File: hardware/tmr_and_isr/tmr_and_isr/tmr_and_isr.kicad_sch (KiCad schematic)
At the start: 21 parts, among them J0 Conn_01x10, J1 Conn_01x10, J2 Conn_01x10, J3 Conn_01x12_Male, U1 74LS04, U2 4072, U3 74LS10, U4 74HC00, U6 74HC00, U7 74LS10

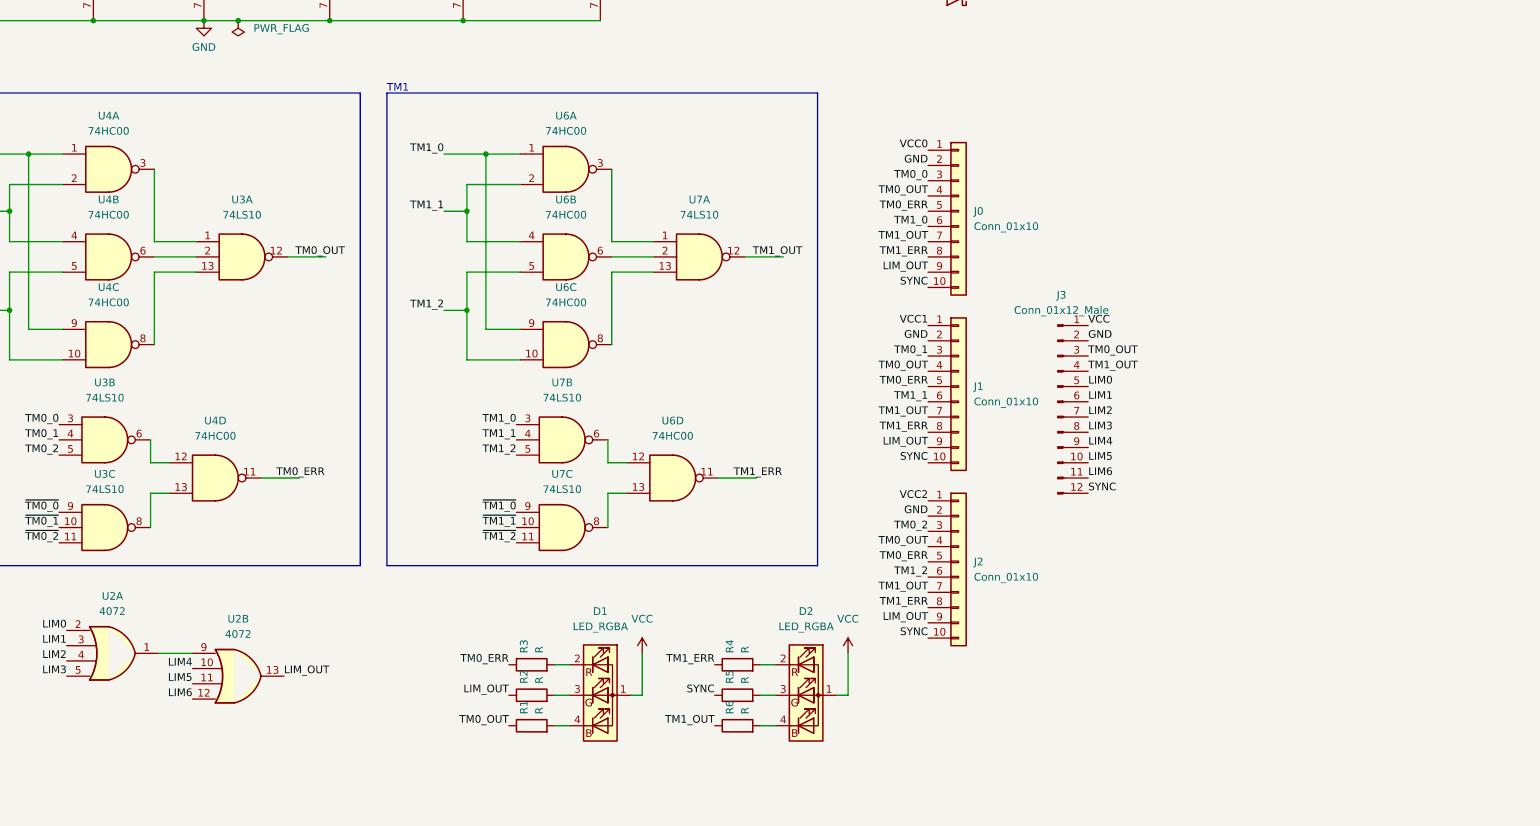
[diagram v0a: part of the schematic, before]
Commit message: Added updated TMR and ISR PCB
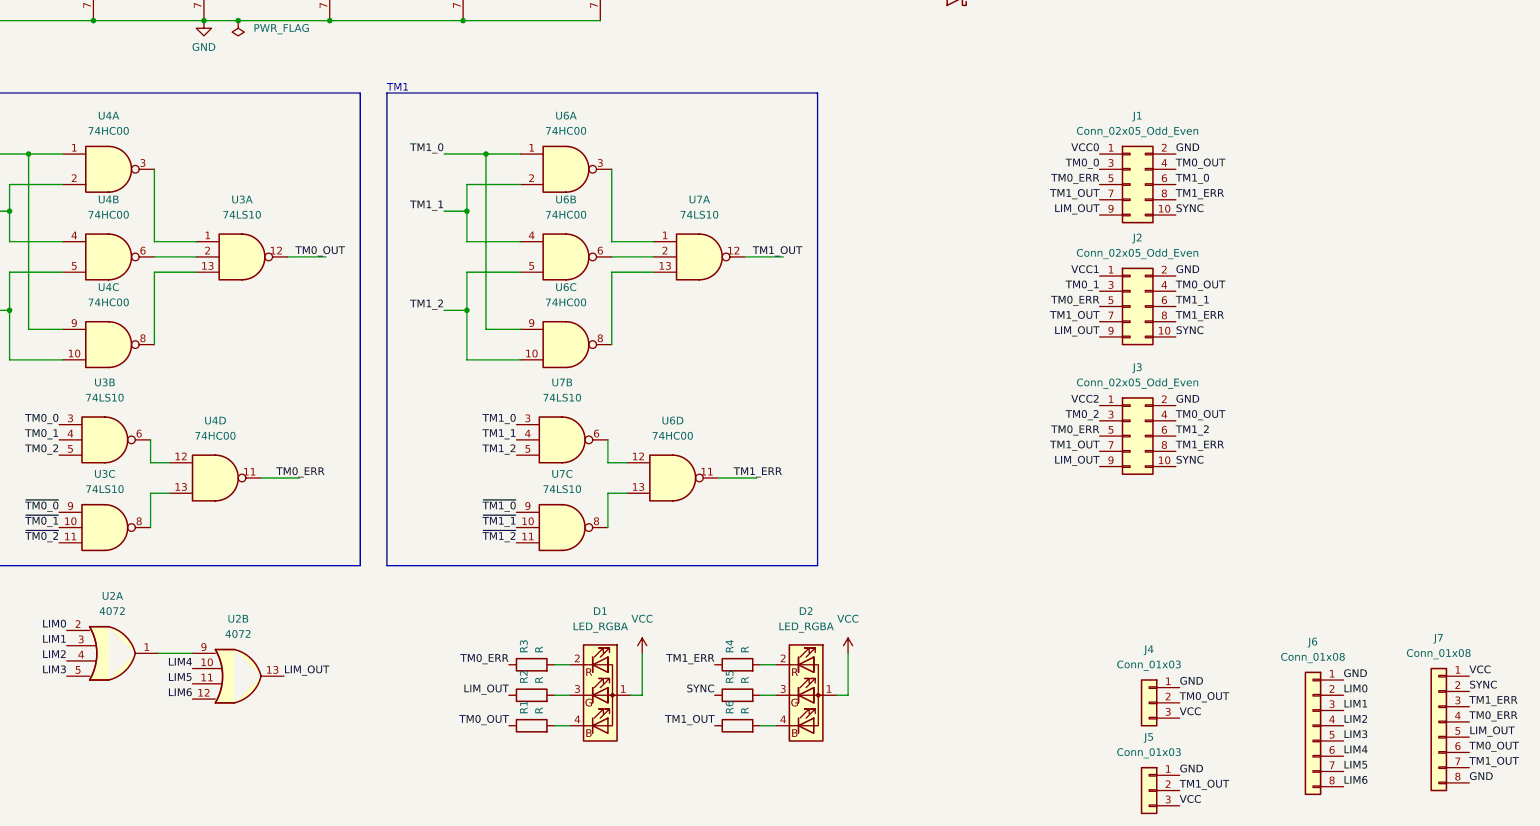
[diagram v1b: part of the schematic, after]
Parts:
- removed J0, J1, J2: Conn_01x10, Connector_JST:JST_PHD_B10B-PHDSS_2x05_P2.00mm_Vertical, symbol Connector_Generic:Conn_01x10
- removed J3: Conn_01x12_Male, Connector_JST:JST_GH_SM12B-GHS-TB_1x12-1MP_P1.25mm_Horizontal, symbol Connector:Conn_01x12_Male
- added J1, J2, J3: Conn_02x05_Odd_Even, Connector_PinSocket_2.54mm:PinSocket_2x05_P2.54mm_Vertical, symbol Connector_Generic:Conn_02x05_Odd_Even
- added J4, J5: Conn_01x03, Connector_JST:JST_PH_B3B-PH-K_1x03_P2.00mm_Vertical, symbol Connector_Generic:Conn_01x03
- added J6, J7: Conn_01x08, Connector_PinHeader_2.54mm:PinHeader_1x08_P2.54mm_Vertical, symbol Connector_Generic:Conn_01x08
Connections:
- net GND: now also J1.2 (Pin_2), J2.2 (Pin_2), J3.2 (Pin_2), J4.1 (Pin_1), J5.1 (Pin_1), J6.1 (Pin_1), J7.8 (Pin_8)
- net LIM0: now also J6.2 (Pin_2)
- net LIM1: now also J6.3 (Pin_3)
- net LIM2: now also J6.4 (Pin_4)
- net LIM3: now also J6.5 (Pin_5)
- net LIM4: now also J6.6 (Pin_6)
- net LIM5: now also J6.7 (Pin_7)
- net LIM6: now also J6.8 (Pin_8)
- net LIM_OUT: now also J1.9 (Pin_9), J2.9 (Pin_9), J3.9 (Pin_9), J7.5 (Pin_5)
- net SYNC: now also J1.10 (Pin_10), J2.10 (Pin_10), J3.10 (Pin_10), J7.2 (Pin_2)
- net TM0_0: now also J1.3 (Pin_3)
- net TM0_1: now also J2.3 (Pin_3)
- net TM0_2: now also J3.3 (Pin_3)
- net TM0_ERR: now also J1.5 (Pin_5), J2.5 (Pin_5), J3.5 (Pin_5), J7.4 (Pin_4)
- net TM0_OUT: now also J1.4 (Pin_4), J2.4 (Pin_4), J3.4 (Pin_4), J4.2 (Pin_2), J7.6 (Pin_6)
- net TM1_0: now also J1.6 (Pin_6)
- net TM1_1: now also J2.6 (Pin_6)
- net TM1_2: now also J3.6 (Pin_6)
- net TM1_ERR: now also J1.8 (Pin_8), J2.8 (Pin_8), J3.8 (Pin_8), J7.3 (Pin_3)
- net TM1_OUT: now also J1.7 (Pin_7), J2.7 (Pin_7), J3.7 (Pin_7), J5.2 (Pin_2), J7.7 (Pin_7)
- net VCC: now also J4.3 (Pin_3), J5.3 (Pin_3), J7.1 (Pin_1)
- net VCC0: now also J1.1 (Pin_1)
- net VCC1: now also J2.1 (Pin_1)
- net VCC2: now also J3.1 (Pin_1)

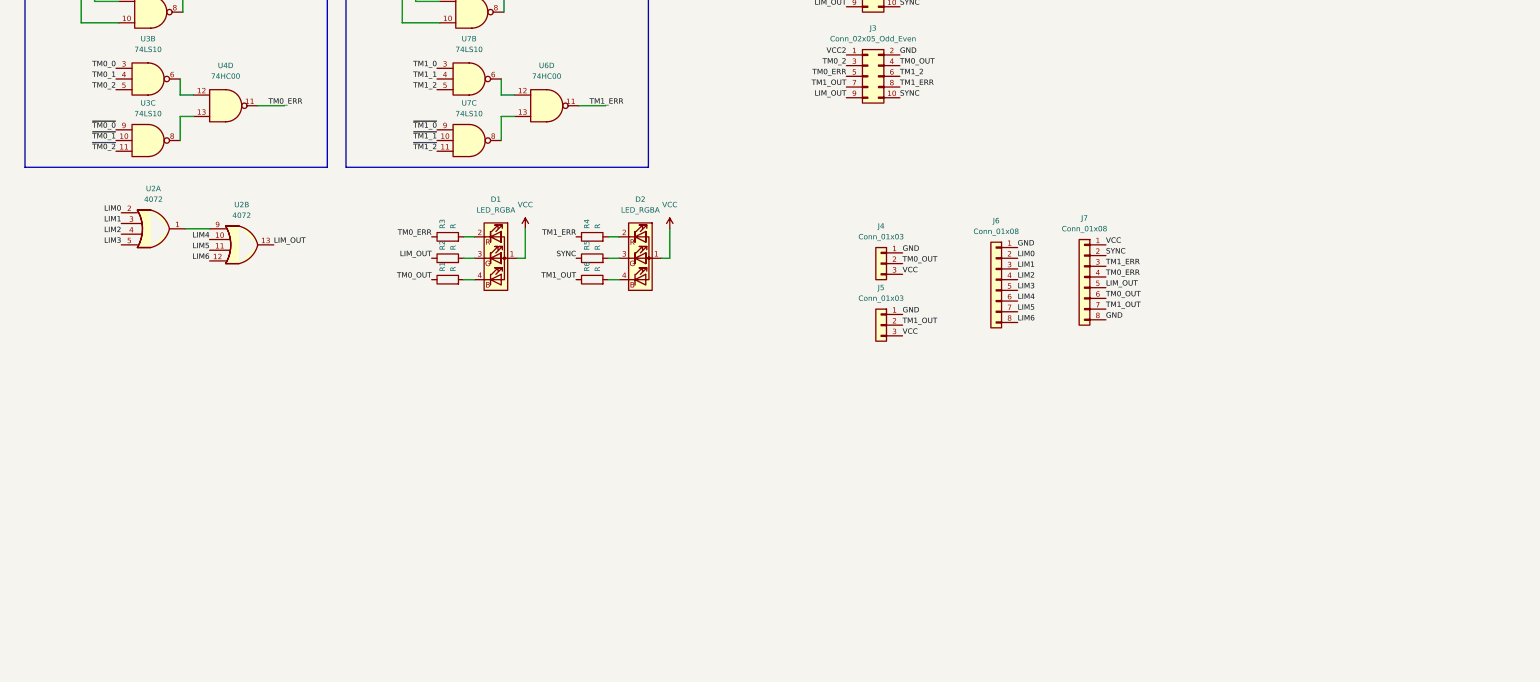
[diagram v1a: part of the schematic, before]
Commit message: Update tmr/isr circuit with TODOs, add tribot webots env vars and auto-switching between webots worlds
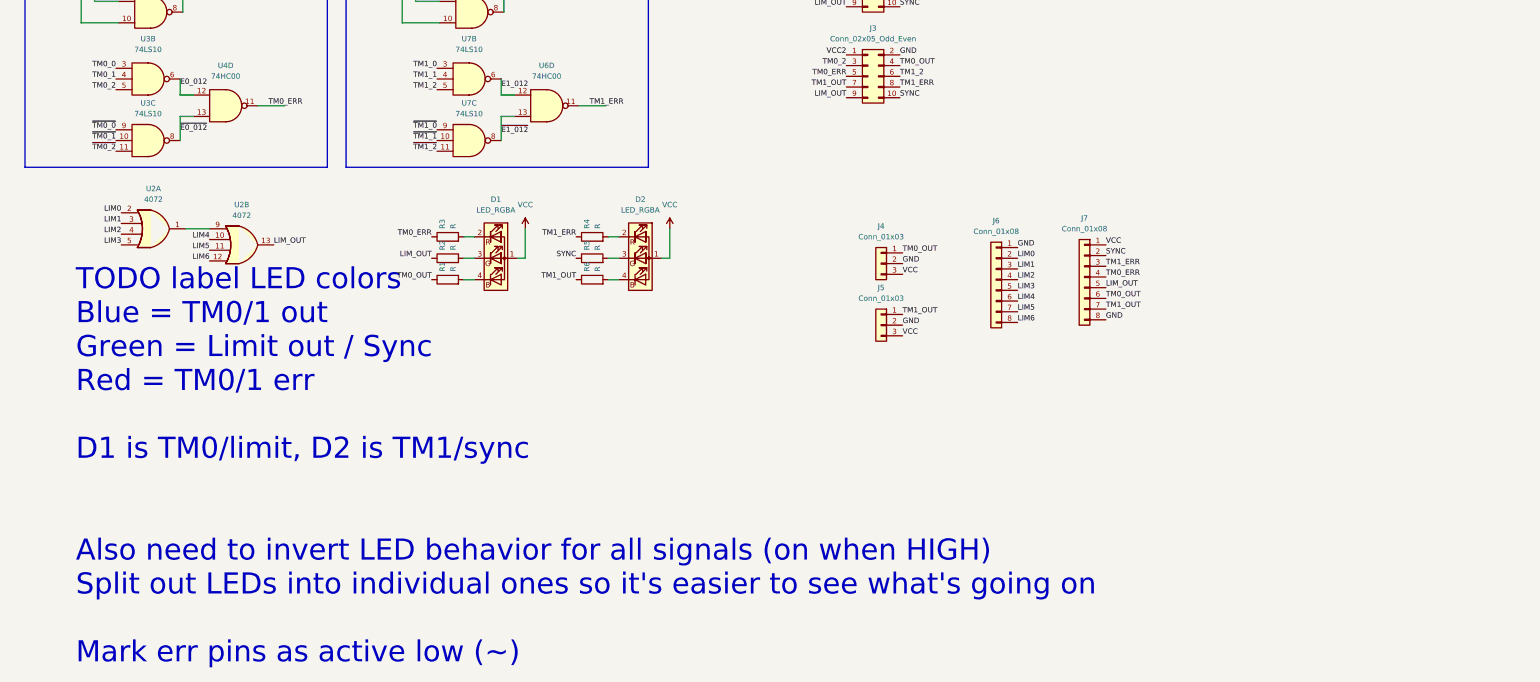
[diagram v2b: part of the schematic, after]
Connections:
- net GND: now also J4.2 (Pin_2), J5.2 (Pin_2); no longer J4.1 (Pin_1), J5.1 (Pin_1)
- net TM0_OUT: now also J4.1 (Pin_1); no longer J4.2 (Pin_2)
- net TM1_OUT: now also J5.1 (Pin_1); no longer J5.2 (Pin_2)
- net E1_012: now reaches U6.12, U7.6
- net ~{E1_012}: now reaches U6.13, U7.8
- net ~{E0_012}: now reaches U3.8, U4.13
- net E0_012: now reaches U3.6, U4.12
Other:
- note added: "TODO label LED colors Blue = TM0/1 out Green = Limit out / Sync Red = TM0/1 err D1 is TM0/limit, D2 is TM1/sync Also need to invert LED behavior for all signals (on when HIGH) Split out LEDs into individual ones so it's easier to see what's going on Mark err pins as active low (~)"
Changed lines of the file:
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@@
     (stroke (width 0) (type default) (color 0 0 0 0))
   )
+  (text "TODO label LED colors\nBlue = TM0/1 out\nGreen = Limit out / Sync\nRed = TM0/1 err\n\nD1 is TM0/limit, D2 is TM1/sync\n\n\nAlso need to invert LED behavior for all signals (on when HIGH)\nSplit out LEDs into individual ones so it's easier to see what's going on\n\nMark err pins as active low (~)"
+    (at 95.885 267.97 0)
+    (effects (font (size 5 5)) (justify left bottom))
+  )
   (text "TM1" (at 160.02 71.12 0)
     (effects (font (size 1.27 1.27)) (justify left bottom))
@@
     (effects (font (size 1.27 1.27)) (justify right bottom))
   )
-  (label "GND" (at 292.1 170.18 0)
-    (effects (font (size 1.27 1.27)) (justify left bottom))
-  )
   (label "TM0_0" (at 278.765 83.82 180)
     (effects (font (size 1.27 1.27)) (justify right bottom))
@@
     (effects (font (size 1.27 1.27)) (justify right bottom))
   )
-  (label "TM1_OUT" (at 292.1 187.325 0)
-    (effects (font (size 1.27 1.27)) (justify left bottom))
-  )
   (label "TM1_OUT" (at 214.63 176.53 180)
     (effects (font (size 1.27 1.27)) (justify right bottom))
@@
     (effects (font (size 1.27 1.27)) (justify right bottom))
   )
+  (label "TM0_OUT" (at 292.1 170.18 0)
+    (effects (font (size 1.27 1.27)) (justify left bottom))
+  )
   (label "TM0_ERR" (at 278.765 128.27 180)
     (effects (font (size 1.27 1.27)) (justify right bottom))
@@
     (effects (font (size 1.27 1.27)) (justify left bottom))
   )
+  (label "E0_012" (at 120.65 130.556 0)
+    (effects (font (size 1.27 1.27)) (justify left bottom))
+  )
   (label "TM0_ERR" (at 278.765 106.68 180)
     (effects (font (size 1.27 1.27)) (justify right bottom))
@@
     (effects (font (size 1.27 1.27)) (justify left bottom))
   )
+  (label "LIM0" (at 319.405 171.45 0)
+    (effects (font (size 1.27 1.27)) (justify left bottom))
+  )
+  (label "TM0_OUT" (at 180.34 176.53 180)
+    (effects (font (size 1.27 1.27)) (justify right bottom))
+  )
+  (label "TM1_0" (at 48.26 118.745 180)
+    (effects (font (size 1.27 1.27)) (justify right bottom))
+  )
+  (label "LIM2" (at 106.68 165.735 180)
+    (effects (font (size 1.27 1.27)) (justify right bottom))
+  )
+  (label "SYNC" (at 214.63 171.45 180)
+    (effects (font (size 1.27 1.27)) (justify right bottom))
+  )
+  (label "LIM2" (at 319.405 176.53 0)
+    (effects (font (size 1.27 1.27)) (justify left bottom))
+  )
+  (label "TM1_0" (at 169.545 81.28 180)
+    (effects (font (size 1.27 1.27)) (justify right bottom))
+  )
+  (label "~{TM0_1}" (at 105.41 143.51 180)
+    (effects (font (size 1.27 1.27)) (justify right bottom))
+  )
+  (label "TM0_1" (at 48.26 88.265 180)
+    (effects (font (size 1.27 1.27)) (justify right bottom))
+  )
+  (label "TM1_ERR" (at 291.465 88.9 0)
+    (effects (font (size 1.27 1.27)) (justify left bottom))
+  )
+  (label "TM1_OUT" (at 278.765 88.9 180)
+    (effects (font (size 1.27 1.27)) (justify right bottom))
+  )
+  (label "~{TM1_1}" (at 181.61 143.51 180)
+    (effects (font (size 1.27 1.27)) (justify right bottom))
+  )
+  (label "TM1_1" (at 291.465 106.68 0)
+    (effects (font (size 1.27 1.27)) (justify left bottom))
+  )
+  (label "GND" (at 291.465 123.19 0)
+    (effects (font (size 1.27 1.27)) (justify left bottom))
+  )
+  (label "TM1_OUT" (at 340.36 183.515 0)
+    (effects (font (size 1.27 1.27)) (justify left bottom))
+  )
+  (label "~{TM1_0}" (at 181.61 140.97 180)
+    (effects (font (size 1.27 1.27)) (justify right bottom))
+  )
+  (label "TM1_2" (at 291.465 128.27 0)
+    (effects (font (size 1.27 1.27)) (justify left bottom))
+  )
+  (label "TM1_2" (at 181.61 131.445 180)
+    (effects (font (size 1.27 1.27)) (justify right bottom))
+  )
+  (label "TM0_OUT" (at 291.465 104.14 0)
+    (effects (font (size 1.27 1.27)) (justify left bottom))
+  )
+  (label "~{E1_012}" (at 196.85 141.986 0)
+    (effects (font (size 1.27 1.27)) (justify left bottom))
+  )
+  (label "TM0_2" (at 93.345 107.315 180)
+    (effects (font (size 1.27 1.27)) (justify right bottom))
+  )
+  (label "LIM_OUT" (at 142.875 168.275 0)
+    (effects (font (size 1.27 1.27)) (justify left bottom))
+  )
+  (label "TM1_2" (at 169.545 107.315 180)
+    (effects (font (size 1.27 1.27)) (justify right bottom))
+  )
+  (label "~{TM1_1}" (at 63.5 134.62 0)
+    (effects (font (size 1.27 1.27)) (justify left bottom))
+  )
   (label "VCC" (at 292.1 175.26 0)
     (effects (font (size 1.27 1.27)) (justify left bottom))
   )
-  (label "LIM0" (at 319.405 171.45 0)
-    (effects (font (size 1.27 1.27)) (justify left bottom))
-  )
-  (label "TM0_OUT" (at 180.34 176.53 180)
-    (effects (font (size 1.27 1.27)) (justify right bottom))
-  )
-  (label "TM1_0" (at 48.26 118.745 180)
-    (effects (font (size 1.27 1.27)) (justify right bottom))
-  )
-  (label "LIM2" (at 106.68 165.735 180)
-    (effects (font (size 1.27 1.27)) (justify right bottom))
-  )
-  (label "SYNC" (at 214.63 171.45 180)
-    (effects (font (size 1.27 1.27)) (justify right bottom))
-  )
-  (label "LIM2" (at 319.405 176.53 0)
-    (effects (font (size 1.27 1.27)) (justify left bottom))
-  )
-  (label "TM1_0" (at 169.545 81.28 180)
-    (effects (font (size 1.27 1.27)) (justify right bottom))
-  )
-  (label "~{TM0_1}" (at 105.41 143.51 180)
-    (effects (font (size 1.27 1.27)) (justify right bottom))
-  )
-  (label "TM0_1" (at 48.26 88.265 180)
-    (effects (font (size 1.27 1.27)) (justify right bottom))
-  )
-  (label "TM1_ERR" (at 291.465 88.9 0)
-    (effects (font (size 1.27 1.27)) (justify left bottom))
-  )
-  (label "TM1_OUT" (at 278.765 88.9 180)
-    (effects (font (size 1.27 1.27)) (justify right bottom))
-  )
-  (label "~{TM1_1}" (at 181.61 143.51 180)
-    (effects (font (size 1.27 1.27)) (justify right bottom))
-  )
-  (label "TM1_1" (at 291.465 106.68 0)
-    (effects (font (size 1.27 1.27)) (justify left bottom))
-  )
-  (label "GND" (at 291.465 123.19 0)
-    (effects (font (size 1.27 1.27)) (justify left bottom))
-  )
-  (label "TM1_OUT" (at 340.36 183.515 0)
-    (effects (font (size 1.27 1.27)) (justify left bottom))
-  )
-  (label "~{TM1_0}" (at 181.61 140.97 180)
-    (effects (font (size 1.27 1.27)) (justify right bottom))
-  )
-  (label "TM1_2" (at 291.465 128.27 0)
-    (effects (font (size 1.27 1.27)) (justify left bottom))
-  )
-  (label "TM1_2" (at 181.61 131.445 180)
-    (effects (font (size 1.27 1.27)) (justify right bottom))
-  )
-  (label "TM0_OUT" (at 291.465 104.14 0)
-    (effects (font (size 1.27 1.27)) (justify left bottom))
-  )
-  (label "TM0_2" (at 93.345 107.315 180)
-    (effects (font (size 1.27 1.27)) (justify right bottom))
-  )
-  (label "LIM_OUT" (at 142.875 168.275 0)
-    (effects (font (size 1.27 1.27)) (justify left bottom))
-  )
-  (label "TM1_2" (at 169.545 107.315 180)
-    (effects (font (size 1.27 1.27)) (justify right bottom))
-  )
-  (label "TM0_OUT" (at 292.1 172.72 0)
-    (effects (font (size 1.27 1.27)) (justify left bottom))
-  )
-  (label "~{TM1_1}" (at 63.5 134.62 0)
-    (effects (font (size 1.27 1.27)) (justify left bottom))
-  )
   (label "TM1_0" (at 291.465 86.36 0)
     (effects (font (size 1.27 1.27)) (justify left bottom))
@@
     (effects (font (size 1.27 1.27)) (justify left bottom))
   )
+  (label "~{E0_012}" (at 120.65 141.478 0)
+    (effects (font (size 1.27 1.27)) (justify left bottom))
+  )
   (label "TM0_ERR" (at 340.36 175.895 0)
     (effects (font (size 1.27 1.27)) (justify left bottom))
   )
+  (label "GND" (at 292.1 172.72 0)
+    (effects (font (size 1.27 1.27)) (justify left bottom))
+  )
   (label "TM0_1" (at 93.345 90.805 180)
     (effects (font (size 1.27 1.27)) (justify right bottom))
@@
     (effects (font (size 1.27 1.27)) (justify left bottom))
   )
+  (label "TM1_OUT" (at 292.1 184.785 0)
+    (effects (font (size 1.27 1.27)) (justify left bottom))
+  )
   (label "LIM4" (at 319.405 181.61 0)
     (effects (font (size 1.27 1.27)) (justify left bottom))
   )
+  (label "GND" (at 292.1 187.325 0)
+    (effects (font (size 1.27 1.27)) (justify left bottom))
+  )
   (label "~{TM1_0}" (at 63.5 118.745 0)
     (effects (font (size 1.27 1.27)) (justify left bottom))
   )
+  (label "E1_012" (at 196.85 131.064 0)
+    (effects (font (size 1.27 1.27)) (justify left bottom))
+  )
   (label "TM0_1" (at 278.765 104.14 180)
     (effects (font (size 1.27 1.27)) (justify right bottom))
@@
     (effects (font (size 1.27 1.27)) (justify left bottom))
   )
-  (label "GND" (at 292.1 184.785 0)
-    (effects (font (size 1.27 1.27)) (justify left bottom))
-  )
